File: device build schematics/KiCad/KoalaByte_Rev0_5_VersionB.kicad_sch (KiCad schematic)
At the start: 0 parts

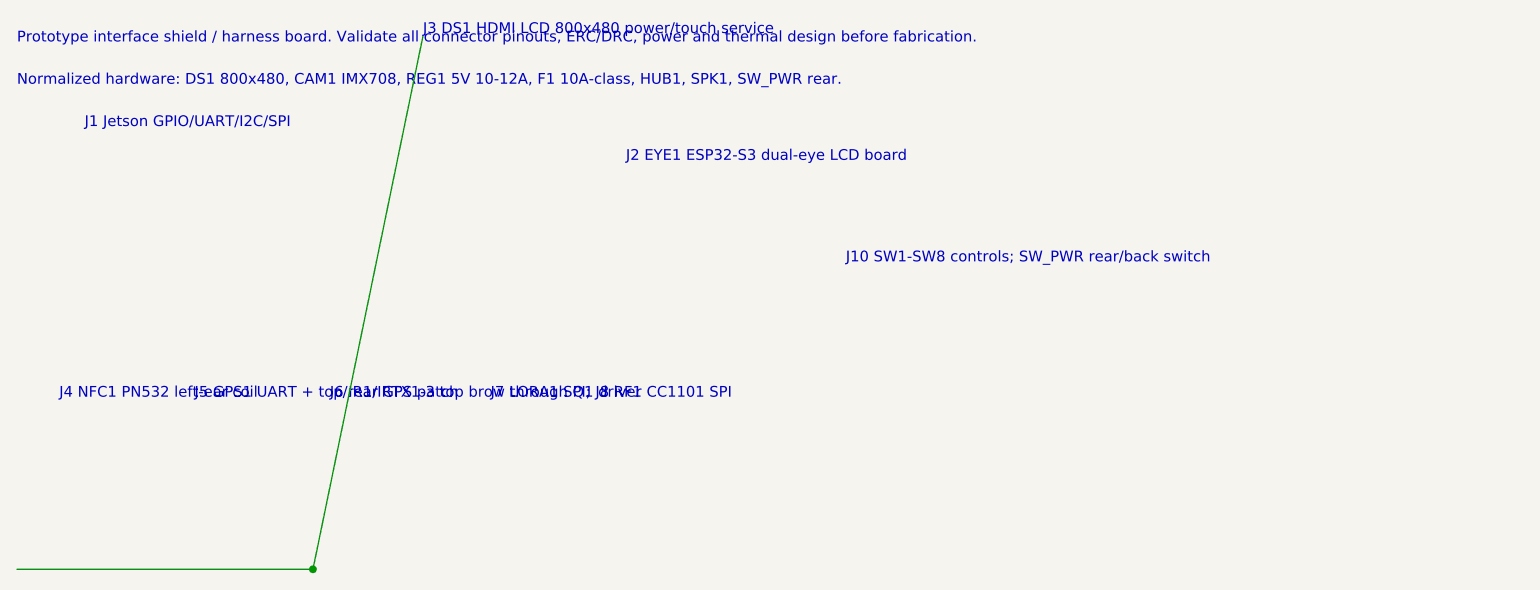
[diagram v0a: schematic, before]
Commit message: Add MIC1 schematic starter annotation
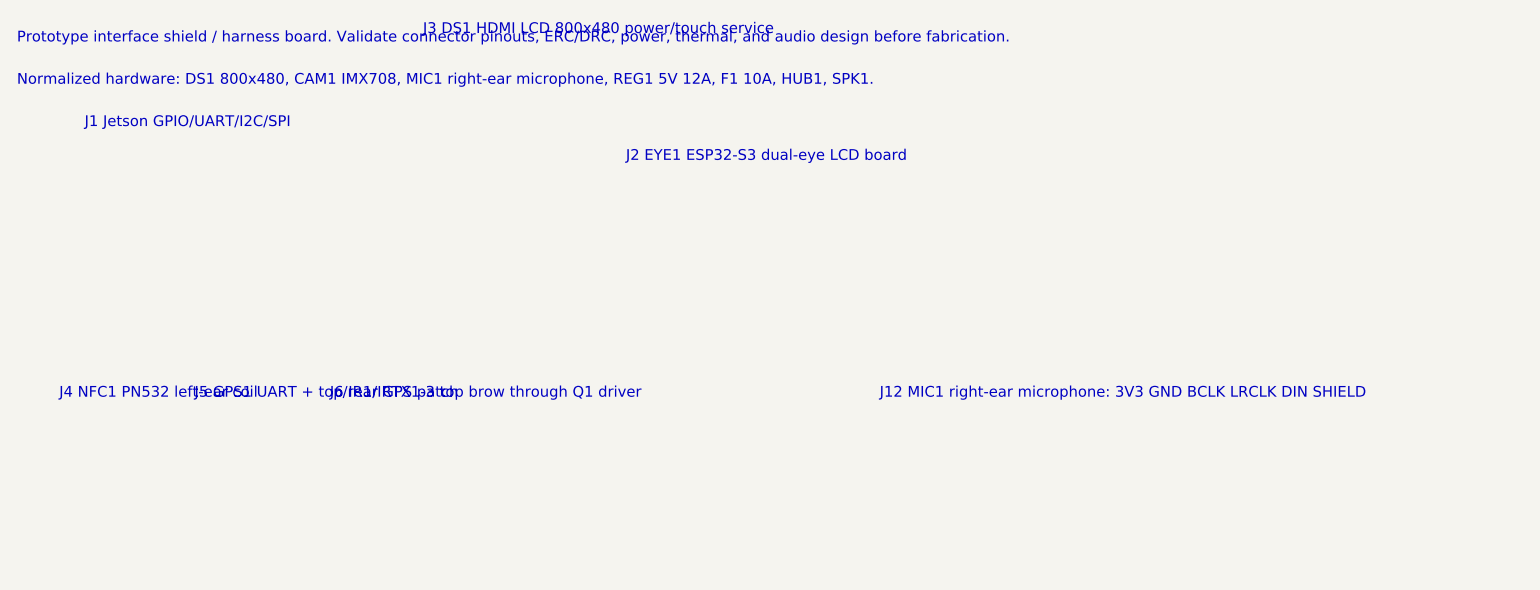
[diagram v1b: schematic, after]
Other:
- note added: "J12 MIC1 right-ear microphone: 3V3 GND BCLK LRCLK DIN SHIELD"
- note added: "Normalized hardware: DS1 800x480, CAM1 IMX708, MIC1 right-ear microphone, REG1 5V 12A, F1 10A, HUB1, SPK1."
- note added: "Prototype interface shield / harness board. Validate connector pinouts, ERC/DRC, power, thermal, and audio design before fabrication."
- note removed: "J10 SW1-SW8 controls; SW_PWR rear/back switch"
- note removed: "J7 LORA1 SPI; J8 RF1 CC1101 SPI"
- note removed: "Normalized hardware: DS1 800x480, CAM1 IMX708, REG1 5V 10-12A, F1 10A-class, HUB1, SPK1, SW_PWR rear."
- note removed: "Prototype interface shield / harness board. Validate all connector pinouts, ERC/DRC, power and thermal design before fabrication."
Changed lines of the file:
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@@
     (rev "0.5B-normalized")
     (company "Urban Poacher / Koalabyte")
-    (comment 1 "CAM1 IMX708 nose-pod CSI camera; DS1 800x480 HDMI display")
-    (comment 2 "REG1 5V 10-12A; F1 10A-class protection; REG2 3V3 logic")
-    (comment 3 "EYE1 ESP32-S3 dual 1.28in IPS LCD board; HUB1 and SPK1 retained")
+    (comment 1 "CAM1 IMX708 centered above eyes; DS1 800x480 HDMI display")
+    (comment 2 "MIC1 right-ear microphone via J12 harness; SPK1 retained")
+    (comment 3 "REG1 5V 12A; F1 10A-class protection; REG2 3V3 logic")
   )
-  (junction (at 45 72) (diameter 0) (color 0 0 0 0))
-  (wire (pts (xy 10 72) (xy 45 72)) (stroke (width 0.25) (type default)))
-  (wire (pts (xy 45 72) (xy 58 9)) (stroke (width 0.25) (type default)))
-  (text "Prototype interface shield / harness board. Validate all connector pinouts, ERC/DRC, power and thermal design before fabrication." (at 10 10 0)
+  (text "Prototype interface shield / harness board. Validate connector pinouts, ERC/DRC, power, thermal, and audio design before fabrication." (at 10 10 0)
     (effects (font (size 1.27 1.27)) (justify left bottom))
   )
-  (text "Normalized hardware: DS1 800x480, CAM1 IMX708, REG1 5V 10-12A, F1 10A-class, HUB1, SPK1, SW_PWR rear." (at 10 15 0)
+  (text "Normalized hardware: DS1 800x480, CAM1 IMX708, MIC1 right-ear microphone, REG1 5V 12A, F1 10A, HUB1, SPK1." (at 10 15 0)
     (effects (font (size 1.27 1.27)) (justify left bottom))
   )
-  (text "J1 Jetson GPIO/UART/I2C/SPI" (at 18 20 0)
-    (effects (font (size 1.27 1.27)) (justify left bottom))
-  )
-  (text "J2 EYE1 ESP32-S3 dual-eye LCD board" (at 82 24 0)
-    (effects (font (size 1.27 1.27)) (justify left bottom))
-  )
-  (text "J3 DS1 HDMI LCD 800x480 power/touch service" (at 58 9 0)
-    (effects (font (size 1.27 1.27)) (justify left bottom))
-  )
-  (text "J4 NFC1 PN532 left-ear coil" (at 15 52 0)
-    (effects (font (size 1.27 1.27)) (justify left bottom))
-  )
-  (text "J5 GPS1 UART + top/rear GPS patch" (at 31 52 0)
-    (effects (font (size 1.27 1.27)) (justify left bottom))
-  )
-  (text "J6 IR1/IRTX1-3 top brow through Q1 driver" (at 47 52 0)
-    (effects (font (size 1.27 1.27)) (justify left bottom))
-  )
-  (text "J7 LORA1 SPI; J8 RF1 CC1101 SPI" (at 66 52 0)
-    (effects (font (size 1.27 1.27)) (justify left bottom))
-  )
-  (text "J10 SW1-SW8 controls; SW_PWR rear/back switch" (at 108 36 0)
-    (effects (font (size 1.27 1.27)) (justify left bottom))
-  )
-  (sheet_instances
-    (path "/" (page "1"))
-  )
+  (text "J1 Jetson GPIO/UART/I2C/SPI" (at 18 20 0) (effects (font (size 1.27 1.27)) (justify left bottom)))
+  (text "J2 EYE1 ESP32-S3 dual-eye LCD board" (at 82 24 0) (effects (font (size 1.27 1.27)) (justify left bottom)))
+  (text "J3 DS1 HDMI LCD 800x480 power/touch service" (at 58 9 0) (effects (font (size 1.27 1.27)) (justify left bottom)))
+  (text "J4 NFC1 PN532 left-ear coil" (at 15 52 0) (effects (font (size 1.27 1.27)) (justify left bottom)))
+  (text "J5 GPS1 UART + top/rear GPS patch" (at 31 52 0) (effects (font (size 1.27 1.27)) (justify left bottom)))
+  (text "J6 IR1/IRTX1-3 top brow through Q1 driver" (at 47 52 0) (effects (font (size 1.27 1.27)) (justify left bottom)))
+  (text "J12 MIC1 right-ear microphone: 3V3 GND BCLK LRCLK DIN SHIELD" (at 112 52 0) (effects (font (size 1.27 1.27)) (justify left bottom)))
+  (sheet_instances (path "/" (page "1")))
 )
